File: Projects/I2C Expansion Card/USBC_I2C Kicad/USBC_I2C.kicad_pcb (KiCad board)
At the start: 2 copper layers, 26 x 30 mm, 26 parts, among them SW1 SW_DIP_x04, U1 MCP2221AxSL

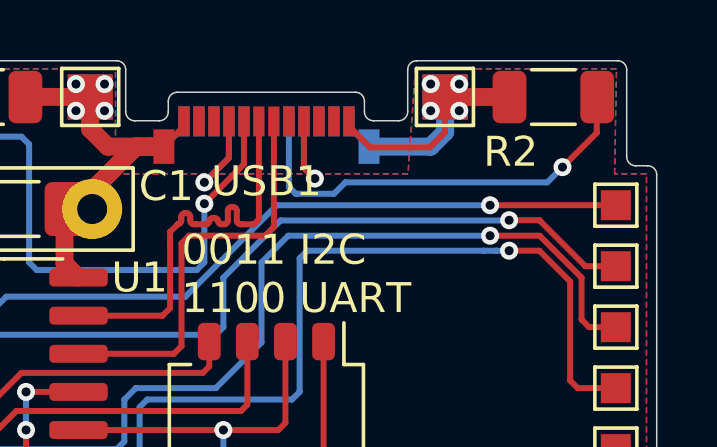
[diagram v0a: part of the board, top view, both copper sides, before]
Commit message: Adding new idea and removing R2 from schematic
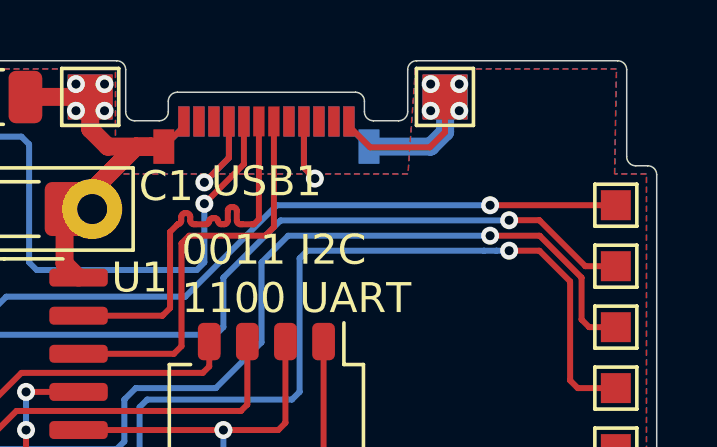
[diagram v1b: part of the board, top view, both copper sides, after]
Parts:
- removed R2: Resistors TBD, Resistor_SMD:R_1206_3216Metric
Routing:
- net Net-(USB1-VCONN): track 14.6 -> 0.00 mm, vias 1 -> 0
- net GND: track 34.7 -> 32.6 mm

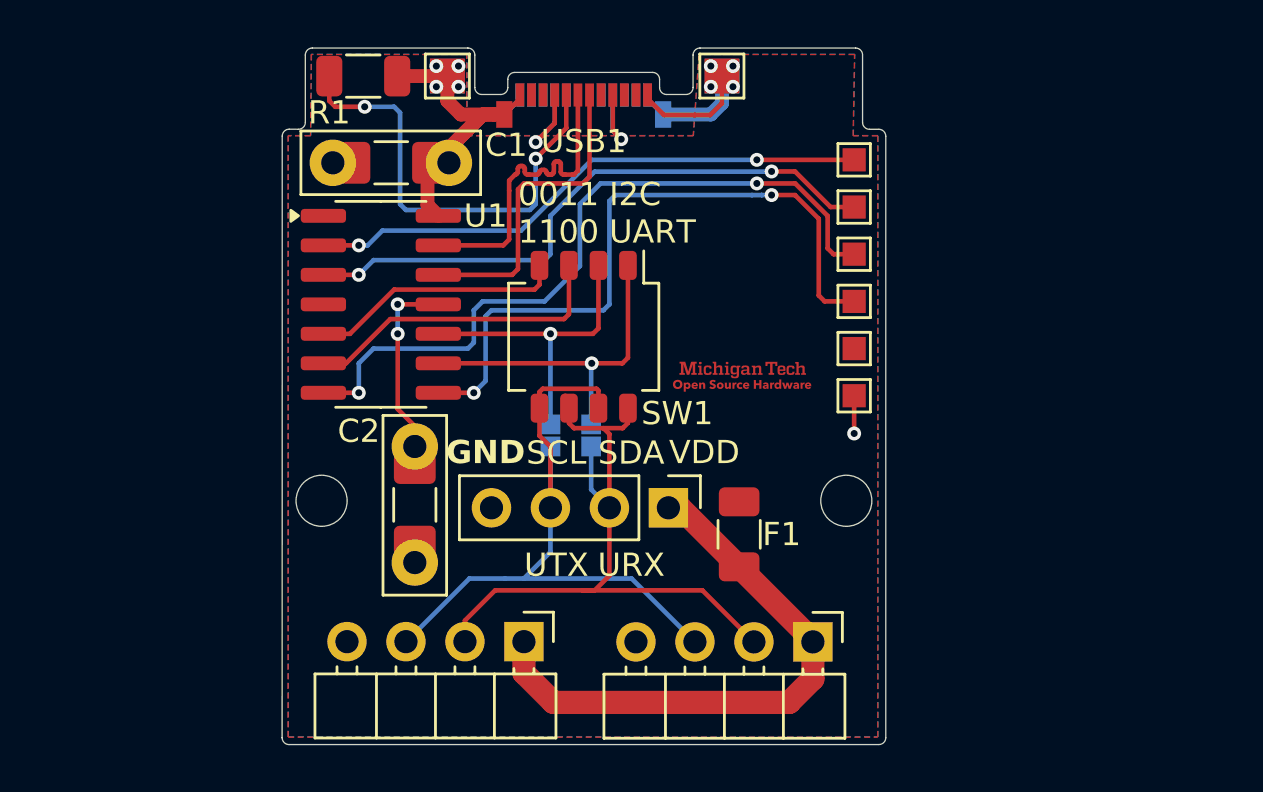
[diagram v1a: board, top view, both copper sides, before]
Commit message: Shortened the board
Shortened the board because of mounting issues when we 3d printed the case to sit flush with the exterior.
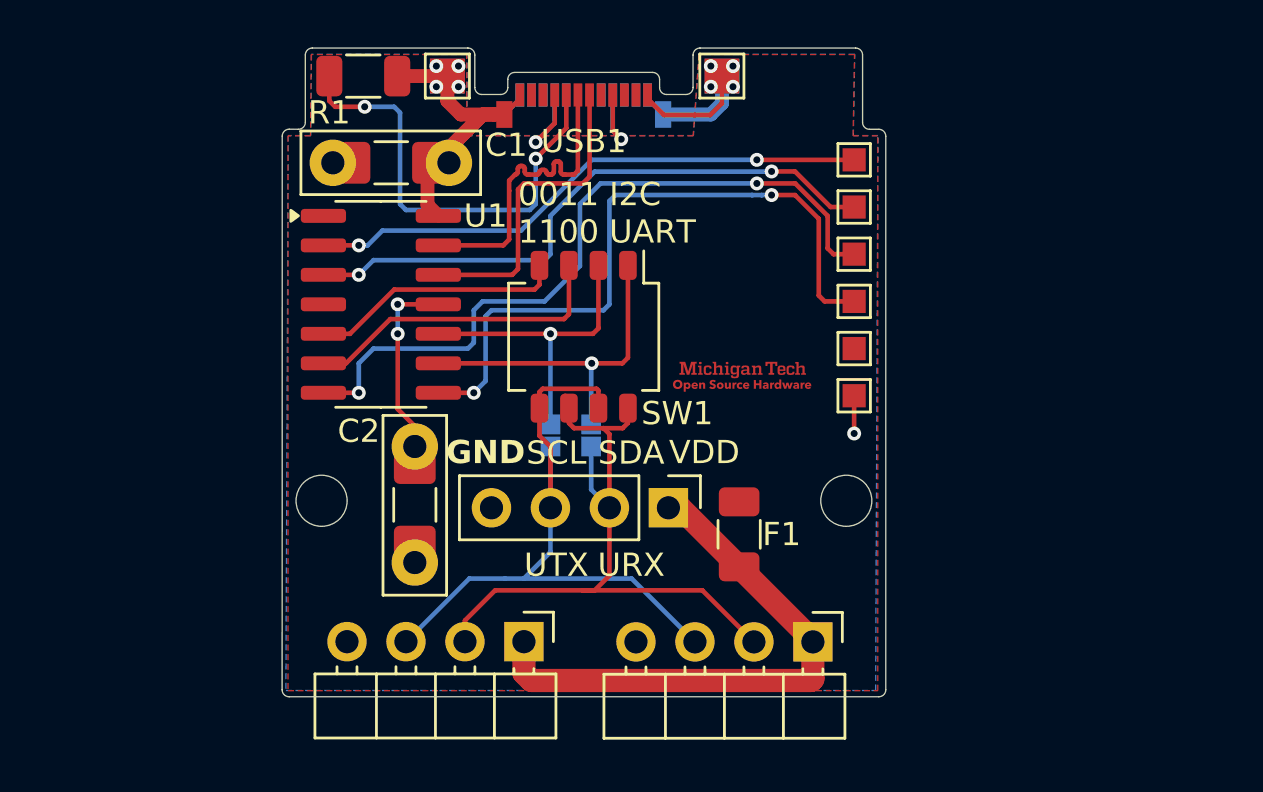
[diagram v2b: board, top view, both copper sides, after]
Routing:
- net Vo: track 25.6 -> 24.8 mm
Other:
- board size 26 x 30 mm -> 26 x 27.9 mm
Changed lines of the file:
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@@
+		(layer "Edge.Cuts")
+	)
+	(gr_arc
+		(start 84.12 85.1)
+		(mid 83.907868 85.012132)
+		(end 83.82 84.8)
+		(stroke
+			(width 0.05)
+			(type solid)
+		)
 		(layer "Edge.Cuts")
 	)
 	(gr_line
-		(start 84.12 87.16)
-		(end 109.52 87.16)
+		(start 84.12 85.1)
+		(end 109.52 85.1)
 		(stroke
 			(width 0.05)
@@
 	)
 	(gr_line
-		(start 109.82 86.86)
+		(start 109.82 84.8)
 		(end 109.82 60.96)
 		(stroke
@@
 	(gr_line
 		(start 83.8248 60.9552)
-		(end 83.82 86.868)
+		(end 83.82 84.8)
 		(stroke
 			(width 0.05)
@@
 	)
 	(gr_arc
-		(start 109.82 86.86)
-		(mid 109.732132 87.072132)
-		(end 109.52 87.16)
+		(start 109.82 84.8)
+		(mid 109.732132 85.012132)
+		(end 109.52 85.1)
 		(stroke
 			(width 0.05)
@@
 			(width 0.05)
 			(type default)
-		)
-		(layer "Edge.Cuts")
-	)
-	(gr_arc
-		(start 84.12 87.16)
-		(mid 83.907868 87.072132)
-		(end 83.82 86.86)
-		(stroke
-			(width 0.05)
-			(type solid)
 		)
 		(layer "Edge.Cuts")
@@
 	)
 	(segment
+		(start 106.608 84.4)
+		(end 94.56 84.4)
+		(width 1)
+		(layer "F.Cu")
+		(net 19)
+	)
+	(segment
 		(start 100.962 76.962)
 		(end 103.505 79.505)
@@
 	(segment
 		(start 106.68 82.737)
-		(end 106.68 84.328)
-		(width 1)
-		(layer "F.Cu")
-		(net 19)
-	)
-	(segment
-		(start 105.664 85.344)
-		(end 95.504 85.344)
-		(width 1)
-		(layer "F.Cu")
-		(net 19)
-	)
-	(segment
-		(start 106.68 82.737)
 		(end 106.68 82.68)
 		(width 1)
@@
 	)
 	(segment
-		(start 106.68 84.328)
-		(end 105.664 85.344)
+		(start 94.56 84.4)
+		(end 94.234 84.074)
+		(width 1)
+		(layer "F.Cu")
+		(net 19)
+	)
+	(segment
+		(start 106.68 82.737)
+		(end 106.68 84.328)
+		(width 1)
+		(layer "F.Cu")
+		(net 19)
+	)
+	(segment
+		(start 100.457 76.962)
+		(end 100.962 76.962)
 		(width 1)
 		(layer "F.Cu")
@@
 	)
 	(segment
-		(start 95.504 85.344)
-		(end 94.234 84.074)
-		(width 1)
-		(layer "F.Cu")
-		(net 19)
-	)
-	(segment
-		(start 100.457 76.962)
-		(end 100.962 76.962)
+		(start 106.68 84.328)
+		(end 106.608 84.4)
 		(width 1)
 		(layer "F.Cu")
@@
 		(polygon
 			(pts
-				(xy 85.074 57.439508) (xy 85.044 60.939508) (xy 84.074 60.939508) (xy 84.074 86.839508) (xy 109.474 86.839508)
+				(xy 85.074 57.439508) (xy 85.044 60.939508) (xy 84.074 60.939508) (xy 84.074 84.839508) (xy 109.474 84.839508)
 				(xy 109.474 60.939508) (xy 108.412 60.939508) (xy 108.474 57.439508) (xy 101.774 57.439508) (xy 101.524 60.939508)
 				(xy 91.774 60.939508) (xy 91.774 57.439508)
@@
 		(polygon
 			(pts
-				(xy 85.0834 57.4294) (xy 85.0534 60.9294) (xy 84.0834 60.9294) (xy 84.0834 86.8294) (xy 109.4834 86.8294)
+				(xy 85.0834 57.4294) (xy 85.0534 60.9294) (xy 84.0834 60.9294) (xy 83.9834 84.8294) (xy 109.3834 84.8294)
 				(xy 109.4834 60.9294) (xy 108.4214 60.9294) (xy 108.4834 57.4294) (xy 101.7834 57.4294) (xy 101.5334 60.9294)
 				(xy 91.7834 60.9294) (xy 91.7834 57.4294)

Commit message: Add OV protection to I2C Card
Also includes changing the length of the board, adding a second power plane (Vo), and moving a couple traces slightly to accomodate all these changes.
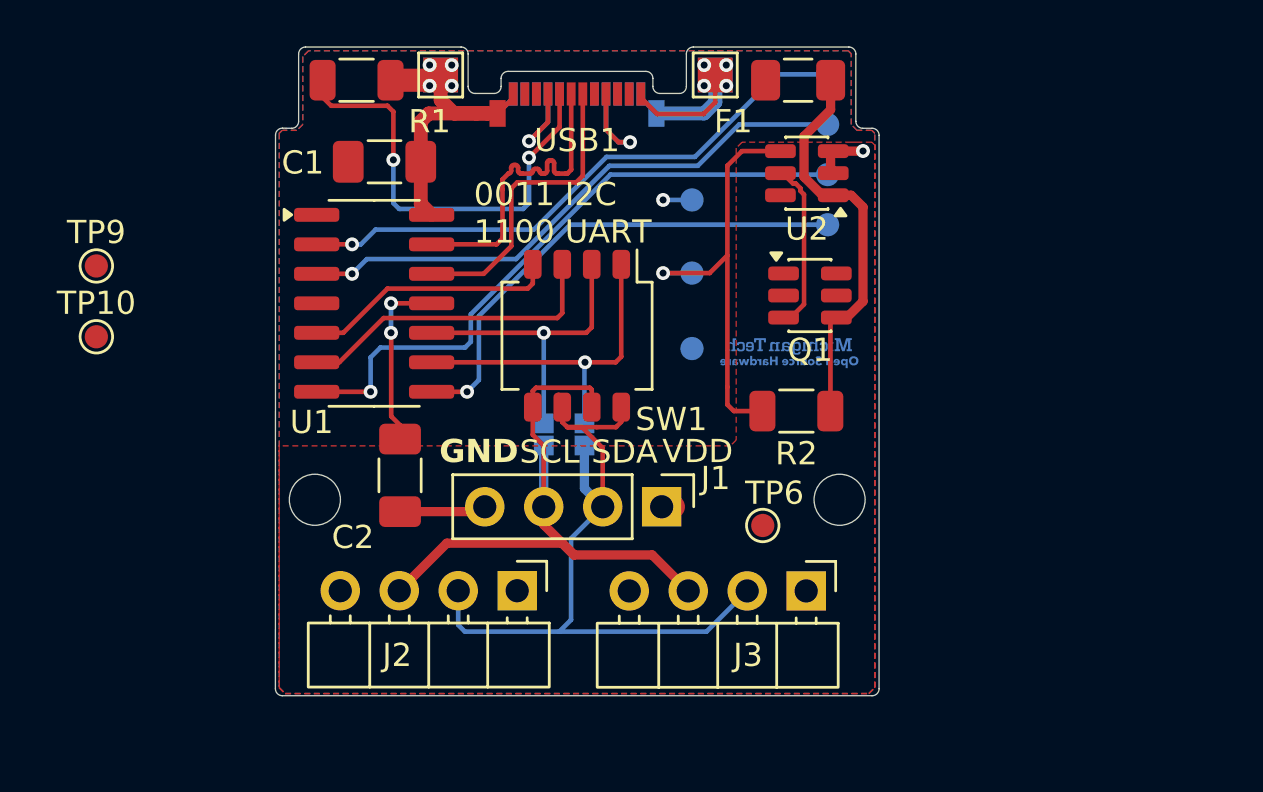
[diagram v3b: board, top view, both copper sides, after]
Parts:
- removed REF** (x2): PinHeader_1x04_P2.54mm_Horizontal, Connector_PinHeader_2.54mm:PinHeader_1x04_P2.54mm_Horizontal
- removed REF** (x6): TestPoint_Pad_1.0x1.0mm, TestPoint:TestPoint_Pad_1.0x1.0mm
- removed REF**: PinHeader_1x04_P2.54mm_Vertical, Connector_PinHeader_2.54mm:PinHeader_1x04_P2.54mm_Vertical
- added J1: 2.54mm Pitch Header, Connector_PinHeader_2.54mm:PinHeader_1x04_P2.54mm_Vertical, F.Cu at (100.2, 76.9)
- added J2: 2.54mm Pitch Header, Connector_PinHeader_2.54mm:PinHeader_1x04_P2.54mm_Horizontal, F.Cu at (93.9, 80.5)
- added J3: 2.54mm Pitch Header, Connector_PinHeader_2.54mm:PinHeader_1x04_P2.54mm_Horizontal, F.Cu at (106.4, 80.5)
- added Q1: DMC2053UVT, Package_TO_SOT_SMD:TSOT-23-6, F.Cu at (106.6, 67.8)
- added R2: 470k, Resistor_SMD:R_1206_3216Metric, F.Cu at (106.0, 72.8)
- added TP1: URx, TestPoint:TestPoint_Pad_D1.0mm, B.Cu at (107.3, 58.3)
- added TP10: D-, TestPoint:TestPoint_Pad_D1.0mm, F.Cu at (75.8, 69.6)
- added TP2: UTx, TestPoint:TestPoint_Pad_D1.0mm, B.Cu at (107.3, 60.5)
- added TP3: USB Status, TestPoint:TestPoint_Pad_D1.0mm, B.Cu at (107.3, 62.6)
- added TP4: I2C Activity, TestPoint:TestPoint_Pad_D1.0mm, B.Cu at (107.3, 64.8)
- added TP5: VBus, TestPoint:TestPoint_Pad_D1.0mm, B.Cu at (101.5, 63.7)
- added TP6: Vo, TestPoint:TestPoint_Pad_D1.0mm, F.Cu at (104.5, 77.7)
- added TP7: GND, TestPoint:TestPoint_Pad_D1.0mm, B.Cu at (101.5, 70.1)
- added TP8: OV Status, TestPoint:TestPoint_Pad_D1.0mm, B.Cu at (101.5, 66.9)
- added TP9: D+, TestPoint:TestPoint_Pad_D1.0mm, F.Cu at (75.8, 66.5)
- added U2: LTC4412xS6, Package_TO_SOT_SMD:TSOT-23-6, F.Cu at (106.4, 62.5)
- G***: moved to B.Cu
- moved F1 19.7 mm to (106.0, 58.5), turned to 0 degrees
- moved G*** 2.27 mm to (105.7, 68.3), turned to 180 degrees
- moved C2 1.42 mm to (88.9, 75.6)
- moved R1 0.34 mm to (87.0, 58.5)
- moved C1 0.29 mm to (88.2, 62.1)
- moved TP3 0.29 mm to (90.6, 58.3)
- moved TP3 0.29 mm to (102.5, 58.3)
- moved USB1 0.29 mm to (96.5, 59.1)
- moved 2x Pads 0.29 mm to (96.8, 73.2)
- moved 2x Pads 0.29 mm to (95.1, 73.2)
- moved ? 0.29 mm to (102.5, 58.3)
- moved ? 0.29 mm to (90.6, 58.3)
- moved H1 0.29 mm to (85.2, 76.6)
- moved H2 0.29 mm to (107.8, 76.6)
- moved SW1 0.29 mm to (96.5, 69.6)
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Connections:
- net Net-(U1-VDD) renamed /VBus
- 2x Pads pad 2: Out0 -> /Out0
- 2x Pads pad 2: Out1 -> /Out1
- F1 pad 2: Vo -> Net-(Q1B-D)
- SW1 pad 5: Out1 -> /SCL/UTx
- SW1 pad 6: Out0 -> /SDA/URx
- SW1 pad 7: Out1 -> /SCL/UTx
- SW1 pad 8: Out0 -> /SDA/URx
- USB1 pad B5: Net-(USB1-VCONN) -> unconnected-(USB1-VCONN-PadB5)
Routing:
- net /Out0: track 0.00 -> 33.2 mm
- net Out0: track 30.5 -> 0.00 mm
- net Out1: track 30.1 -> 0.00 mm
- net /Out1: track 0.00 -> 28.3 mm
- net Vo: track 24.8 -> 0.00 mm
- net Net-(U2-STAT): track 0.00 -> 18.7 mm, vias 0 -> 1
- net Net-(Q1B-D): track 0.00 -> 17.5 mm
- net Net-(U1-GP3): track 29.5 -> 21.6 mm, vias 2 -> 1
- net Net-(Q1B-G): track 0.00 -> 7.68 mm
- net Net-(U1-GP2): track 31.8 -> 27.4 mm, vias 2 -> 1
- net GND: track 32.6 -> 35.4 mm
- net /VBus: track 8.85 -> 11.6 mm, vias 2 -> 3
- net Net-(U1-GP1): track 26.3 -> 24.7 mm, vias 2 -> 1
- net Net-(U1-GP0): track 24.4 -> 25.0 mm, vias 2 -> 1
- net /Vo: track 0.00 -> 0.63 mm
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- added copper zone on F.Cu, net /Vo
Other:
- outline, holes or cut-outs redrawn
- board text added: "SCL"
- board text added: "SDA"
- board text removed: "SCL UTX"
- board text removed: "SDA URX"

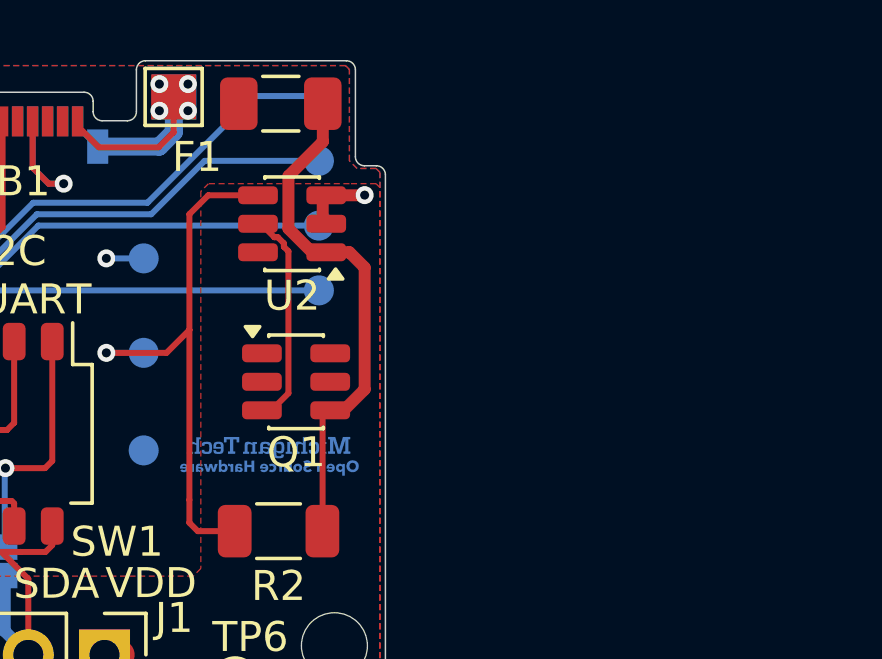
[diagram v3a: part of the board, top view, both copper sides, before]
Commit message: Moved USB port and added OV bypass
Moved USB port on dongle card with preliminary offset. Will update when I have the ports on hand.
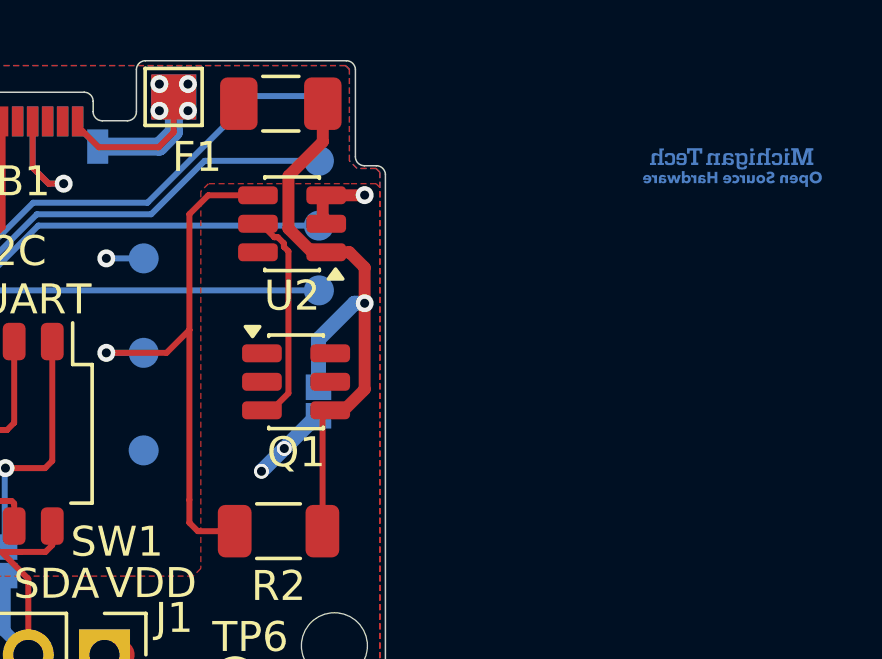
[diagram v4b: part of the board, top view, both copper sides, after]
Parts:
- added 2x Pads: Jumper Pads, Custom Parts:Jumper Pads, B.Cu at (107.3, 67.9)
- moved G*** 18.2 mm to (121.1, 58.7)
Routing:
- net Net-(Q1B-D): track 17.5 -> 21.1 mm, vias 0 -> 1
- net /Vo: track 0.63 -> 3.30 mm, vias 0 -> 2
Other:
- board text added: "OVP Bypass"
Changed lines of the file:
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@@
 		)
 		(embedded_fonts no)
-		(model "${KICAD9_3DMODEL_DIR}/Connector_USB.3dshapes/USB_C_Plug_Molex_105444.step"
+		(model "${KIPRJMOD}/Custom Parts.pretty/1054440001.stp"
 			(offset
-				(xyz 0 0 0)
+				(xyz 0 3.4 -0.425)
 			)
 			(scale
@@
 			)
 			(rotate
-				(xyz 0 0 0)
+				(xyz 90 -0 -0)
 			)
 		)
@@
 	(footprint "LOGO"
 		(layer "B.Cu")
-		(at 105.664 68.326 180)
+		(at 121.1 58.7 180)
 		(property "Reference" "G***"
 			(at 0 0 0)
@@
 		(embedded_fonts no)
 	)
+	(footprint "Custom Parts:Jumper Pads"
+		(layer "B.Cu")
+		(at 107.3 67.9 180)
+		(descr "Through hole straight pin header, 1x02, 1.00mm pitch, single row")
+		(tags "Through hole pin header THT 1x02 1.00mm single row")
+		(property "Reference" "2x Pads"
+			(at 0 1.45 0)
+			(layer "B.SilkS")
+			(hide yes)
+			(effects
+				(font
+					(size 1 1)
+					(thickness 0.15)
+				)
+				(justify mirror)
+			)
+		)
+		(property "Value" "Jumper Pads"
+			(at 0 -2.61 0)
+			(layer "B.Fab")
+			(hide yes)
+			(effects
+				(font
+					(size 1 1)
+					(thickness 0.15)
+				)
+				(justify mirror)
+			)
+		)
+		(property "Datasheet" ""
+			(at 0 0 0)
+			(layer "B.Fab")
+			(hide yes)
+			(effects
+				(font
+					(size 1.27 1.27)
+					(thickness 0.15)
+				)
+				(justify mirror)
+			)
+		)
+		(property "Description" ""
+			(at 0 0 0)
+			(layer "B.Fab")
+			(hide yes)
+			(effects
+				(font
+					(size 1.27 1.27)
+					(thickness 0.15)
+				)
+				(justify mirror)
+			)
+		)
+		(attr through_hole)
+		(fp_line
+			(start 0.581974 0.45)
+			(end 0.577515 -1.61)
+			(stroke
+				(width 0.12)
+				(type solid)
+			)
+			(layer "B.SilkS")
+		)
+		(fp_line
+			(start -0.6 0.45)
+			(end 0.581866 0.45)
+			(stroke
+				(width 0.12)
+				(type solid)
+			)
+			(layer "B.SilkS")
+		)
+		(fp_line
+			(start -0.6 0.45)
+			(end -0.6 -1.61)
+			(stroke
+				(width 0.12)
+				(type solid)
+			)
+			(layer "B.SilkS")
+		)
+		(fp_line
+			(start -0.6 -1.61)
+			(end 0.577515 -1.61)
+			(stroke
+				(width 0.12)
+				(type solid)
+			)
+			(layer "B.SilkS")
+		)
+		(fp_line
+			(start 0.8 0.65)
+			(end -0.85 0.65)
+			(stroke
+				(width 0.05)
+				(type solid)
+			)
+			(layer "B.CrtYd")
+		)
+		(fp_line
+			(start 0.8 -1.8)
+			(end 0.8 0.65)
+			(stroke
+				(width 0.05)
+				(type solid)
+			)
+			(layer "B.CrtYd")
+		)
+		(fp_line
+			(start -0.85 0.65)
+			(end -0.85 -1.8)
+			(stroke
+				(width 0.05)
+				(type solid)
+			)
+			(layer "B.CrtYd")
+		)
+		(fp_line
+			(start -0.85 -1.8)
+			(end 0.8 -1.8)
+			(stroke
+				(width 0.05)
+				(type solid)
+			)
+			(layer "B.CrtYd")
+		)
+		(pad "1" smd rect
+			(at 0 -0.1 180)
+			(size 0.85 0.85)
+			(layers "B.Cu" "B.Mask")
+			(net 5 "Net-(Q1B-D)")
+		)
+		(pad "2" smd rect
+			(at 0 -1.05 180)
+			(size 0.85 0.85)
+			(layers "B.Cu" "B.Mask")
+			(net 7 "/Vo")
+		)
+		(embedded_fonts no)
+		(model "${KICAD9_3DMODEL_DIR}/Connector_PinHeader_1.00mm.3dshapes/PinHeader_1x02_P1.00mm_Vertical.step"
+			(hide yes)
+			(offset
+				(xyz 0 0 0)
+			)
+			(scale
+				(xyz 1 1 1)
+			)
+			(rotate
+				(xyz 0 0 0)
+			)
+		)
+	)
 	(footprint ""
 		(layer "B.Cu")
@@
 		)
 	)
+	(gr_text "OVP Bypass"
+		(at 106 70.8 90)
+		(layer "B.SilkS")
+		(effects
+			(font
+				(size 1 1)
+				(thickness 0.15)
+			)
+			(justify mirror)
+		)
+	)
 	(segment
 		(start 95.27105 59.138)
@@
 	(segment
 		(start 108.839 64.008)
+		(end 108.839 65.2)
+		(width 0.4)
+		(layer "F.Cu")
+		(net 5)
+	)
+	(segment
+		(start 108.839 65.2)
 		(end 108.839 68.072)
 		(width 0.4)
@@
 		(net 5)
 	)
+	(via
+		(at 108.839 65.2)
+		(size 0.6)
+		(drill 0.3)
+		(layers "F.Cu" "B.Cu")
+		(net 5)
+	)
+	(segment
+		(start 108.839 65.2)
+		(end 108.5 65.2)
+		(width 0.5)
+		(layer "B.Cu")
+		(net 5)
+	)
+	(segment
+		(start 107.3 66.4)
+		(end 107.3 68)
+		(width 0.5)
+		(layer "B.Cu")
+		(net 5)
+	)
+	(segment
+		(start 108.5 65.2)
+		(end 107.3 66.4)
+		(width 0.5)
+		(layer "B.Cu")
+		(net 5)
+	)
 	(segment
 		(start 93.05605 65.615)
@@
 		(net 7)
 	)
+	(via
+		(at 106.159621 70.040379)
+		(size 0.5)
+		(drill 0.3)
+		(layers "F.Cu" "B.Cu")
+		(net 7)
+	)
+	(via
+		(at 105.4 70.8)
+		(size 0.5)
+		(drill 0.3)
+		(layers "F.Cu" "B.Cu")
+		(net 7)
+	)
+	(segment
+		(start 107.25 68.95)
+		(end 107.3 68.95)
+		(width 0.5)
+		(layer "B.Cu")
+		(net 7)
+	)
+	(segment
+		(start 106.159621 70.040379)
+		(end 107.25 68.95)
+		(width 0.5)
+		(layer "B.Cu")
+		(net 7)
+	)
+	(segment
+		(start 106.159621 70.040379)
+		(end 105.4 70.8)
+		(width 0.5)
+		(layer "B.Cu")
+		(net 7)
+	)
